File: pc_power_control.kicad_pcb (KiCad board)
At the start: 2 copper layers, 25 x 40 mm, 16 parts, among them IC1 NSVBC847BDW1T2G, J1 JFP1, J2 Conn_Serial, SW1 Reset, SW2 Flash, U1 ESP-12E

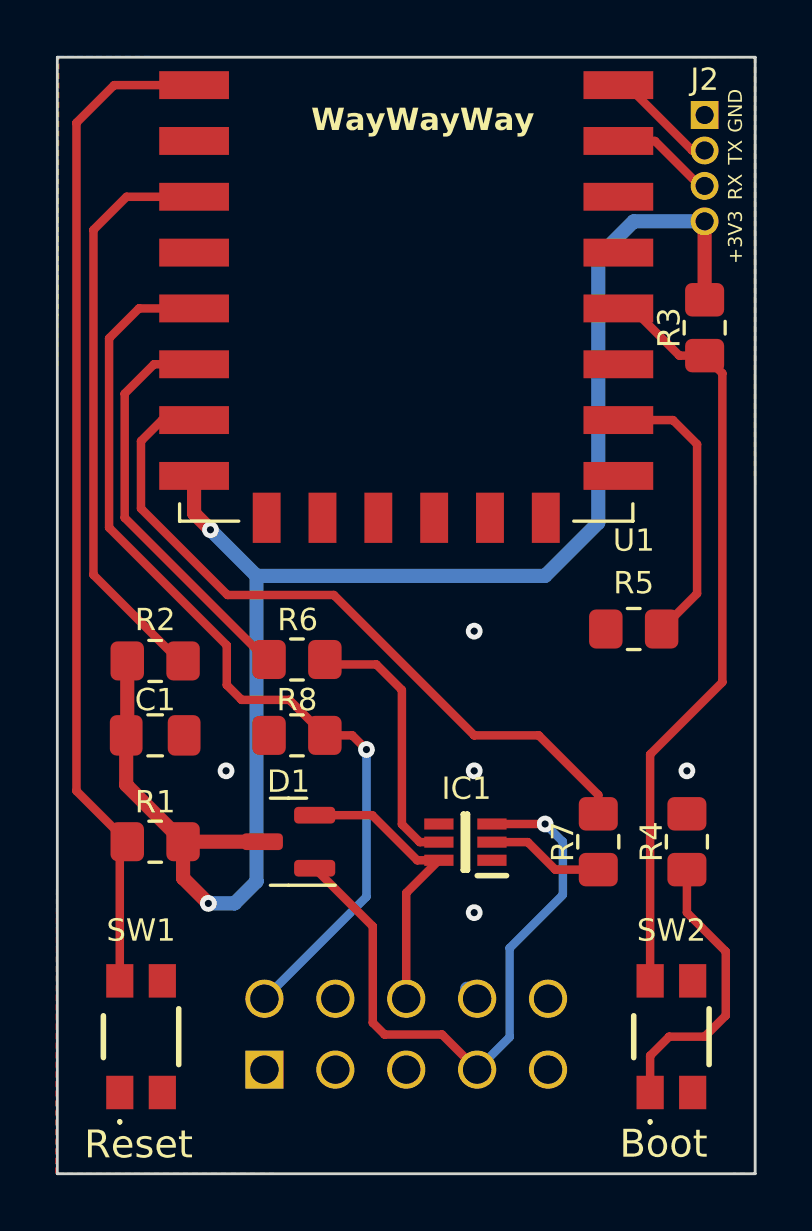
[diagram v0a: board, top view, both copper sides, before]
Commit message: fixed button pin assignment
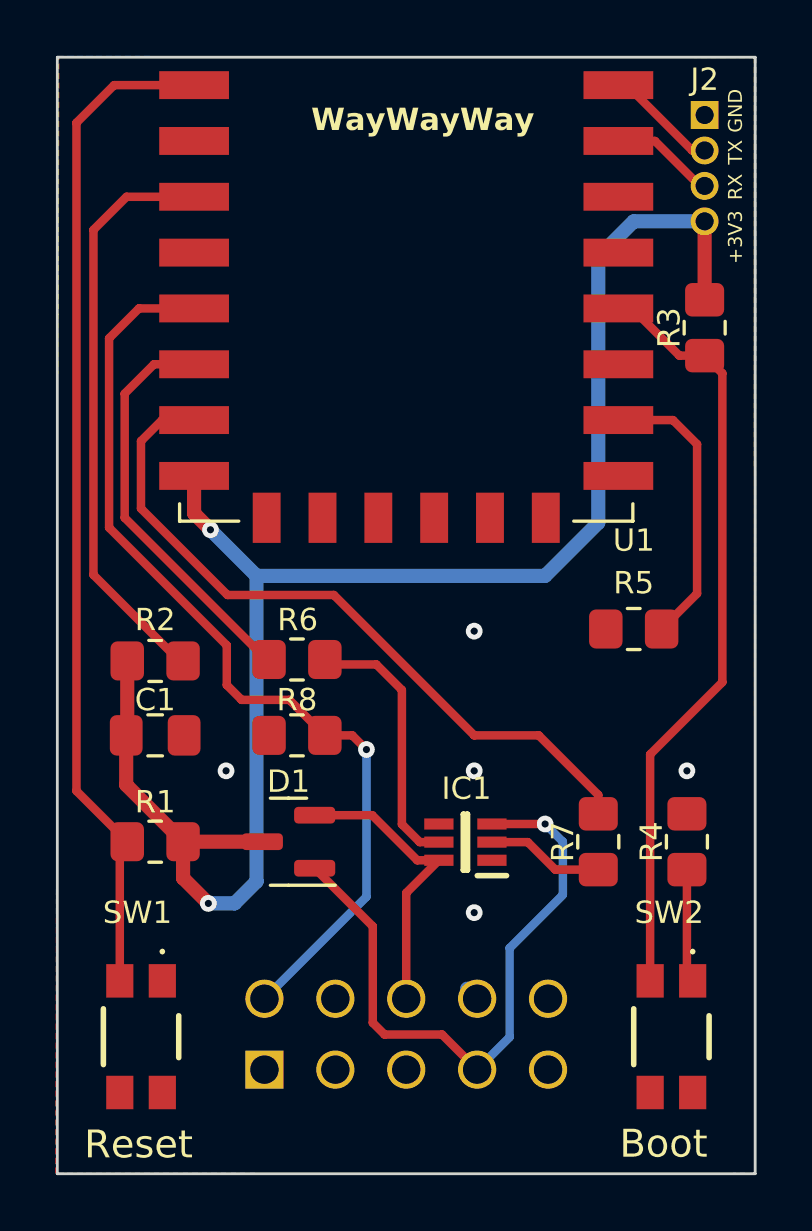
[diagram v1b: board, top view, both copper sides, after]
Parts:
- turned SW1 to -90 degrees
- turned SW2 to -90 degrees
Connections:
- SW1 pad 2: Net-(SW1-B) -> (no net)
- SW1 pad 3: (no net) -> Net-(SW1-B)
- SW2 pad 2: gpio0 -> (no net)
- SW2 pad 3: (no net) -> gpio0
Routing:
- net Net-(SW2-A): track 10.4 -> 4.07 mm
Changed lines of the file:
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@@
   )
   (footprint "Samacsys:RKC2SJF170SMTRLFS" (layer "F.Cu")
-    (at 103 85.09 90)
+    (at 103 85.09 -90)
     (descr "RKC2SJF170SMTR LFS-1")
     (tags "Switch")
@@
     (property "ki_keywords" "switch lever")
     (attr smd)
-    (fp_text reference "SW1" (at 3.81 -0.000004) (layer "F.SilkS")
+    (fp_text reference "SW1" (at -4.445 0.13) (layer "F.SilkS")
         (effects (font (size 0.8 0.8) (thickness 0.15)))
     )
@@
     (fp_line (start 1.75 1.35) (end 1.75 -1.35)
       (stroke (width 0.1) (type solid)) (layer "F.Fab"))
-    (pad "1" smd rect (at -2 -0.762 180) (size 0.975 1.2) (layers "F.Cu" "F.Paste" "F.Mask")
+    (pad "1" smd rect (at -2 -0.762) (size 0.975 1.2) (layers "F.Cu" "F.Paste" "F.Mask")
       (net 1 "GND") (pinfunction "A") (pintype "passive"))
-    (pad "2" smd rect (at 2 -0.762 180) (size 0.975 1.2) (layers "F.Cu" "F.Paste" "F.Mask")
+    (pad "2" smd rect (at 2 -0.762) (size 0.975 1.2) (layers "F.Cu" "F.Paste" "F.Mask"))
+    (pad "3" smd rect (at -2 0.762) (size 0.975 1.2) (layers "F.Cu" "F.Paste" "F.Mask")
       (net 9 "Net-(SW1-B)") (pinfunction "B") (pintype "passive"))
-    (pad "3" smd rect (at -2 0.762 180) (size 0.975 1.2) (layers "F.Cu" "F.Paste" "F.Mask"))
-    (pad "4" smd rect (at 2 0.762 180) (size 0.975 1.2) (layers "F.Cu" "F.Paste" "F.Mask"))
+    (pad "4" smd rect (at 2 0.762) (size 0.975 1.2) (layers "F.Cu" "F.Paste" "F.Mask"))
     (model "${KICAD7_3RD_PARTY}/Samacsys.3dshapes/RKC2SJF170SMTR_LFS.step"
       (offset (xyz 0 0 0))
@@
   )
   (footprint "Samacsys:RKC2SJF170SMTRLFS" (layer "F.Cu")
-    (at 122 85.09 90)
+    (at 122 85.09 -90)
     (descr "RKC2SJF170SMTR LFS-1")
     (tags "Switch")
@@
     (property "ki_keywords" "switch lever")
     (attr smd)
-    (fp_text reference "SW2" (at 3.81 -0.000004) (layer "F.SilkS")
+    (fp_text reference "SW2" (at -4.445 0.08) (layer "F.SilkS")
         (effects (font (size 0.8 0.8) (thickness 0.15)))
     )
@@
     (fp_line (start 1.75 1.35) (end 1.75 -1.35)
       (stroke (width 0.1) (type solid)) (layer "F.Fab"))
-    (pad "1" smd rect (at -2 -0.762 180) (size 0.975 1.2) (layers "F.Cu" "F.Paste" "F.Mask")
+    (pad "1" smd rect (at -2 -0.762) (size 0.975 1.2) (layers "F.Cu" "F.Paste" "F.Mask")
       (net 30 "Net-(SW2-A)") (pinfunction "A") (pintype "passive"))
-    (pad "2" smd rect (at 2 -0.762 180) (size 0.975 1.2) (layers "F.Cu" "F.Paste" "F.Mask")
+    (pad "2" smd rect (at 2 -0.762) (size 0.975 1.2) (layers "F.Cu" "F.Paste" "F.Mask"))
+    (pad "3" smd rect (at -2 0.762) (size 0.975 1.2) (layers "F.Cu" "F.Paste" "F.Mask")
       (net 24 "gpio0") (pinfunction "B") (pintype "passive"))
-    (pad "3" smd rect (at -2 0.762 180) (size 0.975 1.2) (layers "F.Cu" "F.Paste" "F.Mask"))
-    (pad "4" smd rect (at 2 0.762 180) (size 0.975 1.2) (layers "F.Cu" "F.Paste" "F.Mask"))
+    (pad "4" smd rect (at 2 0.762) (size 0.975 1.2) (layers "F.Cu" "F.Paste" "F.Mask"))
     (model "${KICAD7_3RD_PARTY}/Samacsys.3dshapes/RKC2SJF170SMTR_LFS.step"
       (offset (xyz 0 0 0))
@@
     (effects (font (size 0.5 0.5) (thickness 0.15)) (justify left bottom))
   )
-  (gr_text_box "PPC v1.2 Florian Hye"
+  (gr_text_box "PPC v1.3 Florian Hye"
     (start 106.045 87.757) (end 118.985079 89.662) (layer "F.SilkS")
       (effects (font (size 0.7 0.7) (thickness 0.15)) (justify left top))
@@
   (segment (start 100.6856 76.2856) (end 102.505 78.105) (width 0.3048) (layer "F.Cu") (net 9))
   (segment (start 104.9 51) (end 102.035 51) (width 0.3048) (layer "F.Cu") (net 9))
-  (segment (start 102.505 78.105) (end 102.238 78.372) (width 0.3048) (layer "F.Cu") (net 9))
-  (segment (start 102.238 78.372) (end 102.238 83.09) (width 0.3048) (layer "F.Cu") (net 9))
   (segment (start 102.035 51) (end 100.6856 52.3494) (width 0.3048) (layer "F.Cu") (net 9))
   (segment (start 100.6856 52.3494) (end 100.6856 76.2856) (width 0.3048) (layer "F.Cu") (net 9))
+  (segment (start 102.238 78.372) (end 102.238 83.09) (width 0.3048) (layer "F.Cu") (net 9))
+  (segment (start 102.505 78.105) (end 102.238 78.372) (width 0.3048) (layer "F.Cu") (net 9))
   (segment (start 101.2952 56.1848) (end 102.48 55) (width 0.3048) (layer "F.Cu") (net 11))
   (segment (start 104.505 71.628) (end 104.378 71.628) (width 0.3048) (layer "F.Cu") (net 11))
@@
   (segment (start 122.055 63) (end 120.1 63) (width 0.3048) (layer "F.Cu") (net 22))
   (segment (start 122.92 63.865) (end 122.92 69.215) (width 0.3048) (layer "F.Cu") (net 22))
-  (segment (start 123.825 61.325) (end 123.19 60.69) (width 0.3048) (layer "F.Cu") (net 24))
   (segment (start 120.1 59) (end 120.595 59) (width 0.3048) (layer "F.Cu") (net 24))
-  (segment (start 121.238 83.09) (end 121.238 74.977) (width 0.3048) (layer "F.Cu") (net 24))
-  (segment (start 121.238 74.977) (end 123.825 72.39) (width 0.3048) (layer "F.Cu") (net 24))
-  (segment (start 123.825 72.39) (end 123.825 61.325) (width 0.3048) (layer "F.Cu") (net 24))
+  (segment (start 123.19 60.69) (end 123.825 61.325) (width 0.3048) (layer "F.Cu") (net 24))
+  (segment (start 123.825 72.39) (end 121.238 74.977) (width 0.3048) (layer "F.Cu") (net 24))
+  (segment (start 123.825 61.325) (end 123.825 72.39) (width 0.3048) (layer "F.Cu") (net 24))
+  (segment (start 121.238 74.977) (end 121.238 83.09) (width 0.3048) (layer "F.Cu") (net 24))
   (segment (start 122.285 60.69) (end 123.19 60.69) (width 0.3048) (layer "F.Cu") (net 24))
   (segment (start 120.595 59) (end 122.285 60.69) (width 0.3048) (layer "F.Cu") (net 24))
@@
   (segment (start 111.0742 80.0758) (end 107.42 83.73) (width 0.3048) (layer "B.Cu") (net 29))
   (segment (start 111.0742 74.803) (end 111.0742 80.0758) (width 0.3048) (layer "B.Cu") (net 29))
-  (segment (start 123.947261 82.037261) (end 122.555 80.645) (width 0.3048) (layer "F.Cu") (net 30))
-  (segment (start 121.92 85.09) (end 123.19 85.09) (width 0.3048) (layer "F.Cu") (net 30))
-  (segment (start 121.238 85.772) (end 121.92 85.09) (width 0.3048) (layer "F.Cu") (net 30))
-  (segment (start 122.555 80.645) (end 122.555 79.105) (width 0.3048) (layer "F.Cu") (net 30))
-  (segment (start 121.238 87.09) (end 121.238 85.772) (width 0.3048) (layer "F.Cu") (net 30))
-  (segment (start 123.19 85.09) (end 123.947261 84.332739) (width 0.3048) (layer "F.Cu") (net 30))
-  (segment (start 123.947261 84.332739) (end 123.947261 82.037261) (width 0.3048) (layer "F.Cu") (net 30))
+  (segment (start 122.555 82.883) (end 122.762 83.09) (width 0.3048) (layer "F.Cu") (net 30))
+  (segment (start 122.555 79.105) (end 122.555 82.883) (width 0.3048) (layer "F.Cu") (net 30))
   (segment (start 121.40941 53) (end 123.01941 54.61) (width 0.3048) (layer "F.Cu") (net 31))
   (segment (start 120.1 53) (end 121.40941 53) (width 0.3048) (layer "F.Cu") (net 31))
